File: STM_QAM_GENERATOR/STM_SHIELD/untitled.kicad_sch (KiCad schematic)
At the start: 1 part, among them U1 NUCLEO-F446RE

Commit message: STM_SHIELD_DONE
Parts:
- added D1, D2, D3, D4: LED, LED_SMD:LED_0603_1608Metric_Pad1.05x0.95mm_HandSolder, symbol Device:LED
- added J3: Conn_01x08_Socket, Connector_PinSocket_2.54mm:PinSocket_1x08_P2.54mm_Vertical, symbol Connector:Conn_01x08_Socket
- added R28, R29, R30, R31: R, Resistor_SMD:R_0603_1608Metric_Pad0.98x0.95mm_HandSolder, symbol Device:R
- added R35: DNP, Resistor_SMD:R_0603_1608Metric_Pad0.98x0.95mm_HandSolder, symbol Device:R
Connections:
- net CN6_GND is gone; now on net CN10_GND: U1.CN6_6 (CN6_GND), U1.CN6_7 (CN6_GND)
- net CN7_GND is gone; now on net CN10_GND: U1.CN7_19 (CN7_GND), U1.CN7_20 (CN7_GND), U1.CN7_22 (CN7_GND), U1.CN7_8 (CN7_GND)
- net CN10_GND: now also U1.CN5_7 (CN5_GND), R28.1, R29.1, R30.1, R31.1, R35.2
- net at U1.CN5_1 (D8): now also J3.8 (Pin_8)
- net at U1.CN5_10 (D15): now also J3.1 (Pin_1)
- net at U1.CN5_2 (D9): now also J3.7 (Pin_7)
- net at U1.CN5_3 (D10): now also J3.6 (Pin_6)
- net at U1.CN5_4 (D11): now also J3.5 (Pin_5)
- net at U1.CN5_5 (D12): now also J3.4 (Pin_4)
- net at U1.CN5_6 (D13): now also J3.3 (Pin_3)
- net at U1.CN5_9 (D14): now also J3.2 (Pin_2)
- net +5V: now reaches U1.CN6_5 (CN6_+5V)
- net RX/TX: now reaches U1.CN10_1 (PC9)
- net DAC_Q: now reaches U1.CN10_11 (PA5)
- net at U1.CN10_22 (PB2): now also D2.2 (A)
- net at U1.CN10_24 (PB1): now also D1.2 (A)
- net at U1.CN10_27 (PB4): now also D4.2 (A)
- net at U1.CN10_31 (PB3): now also D3.2 (A)
- net at U1.CN10_32 (AGND): now also R35.1
- net ADC_I: now reaches U1.CN7_28 (PA0)
- net ADC_Q: now reaches U1.CN7_30 (PA1)
- net DAC_I: now reaches U1.CN7_32 (PA4)
- new net: D4.1 (K), R31.2
- new net: D2.1 (K), R29.2
- new net: D3.1 (K), R30.2
- new net: D1.1 (K), R28.2

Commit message: Added values to schematics
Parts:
- R28, R29, R30, R31: value R -> 470
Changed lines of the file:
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@@
 			)
 		)
-		(property "Value" "R"
+		(property "Value" "470"
 			(at 114.3 82.55 90)
 			(effects
@@
 			)
 		)
-		(property "Value" "R"
+		(property "Value" "470"
 			(at 114.3 77.47 90)
 			(effects
@@
 			)
 		)
-		(property "Value" "R"
+		(property "Value" "470"
 			(at 114.3 74.93 90)
 			(effects
@@
 			)
 		)
-		(property "Value" "R"
+		(property "Value" "470"
 			(at 114.3 80.01 90)
 			(effects

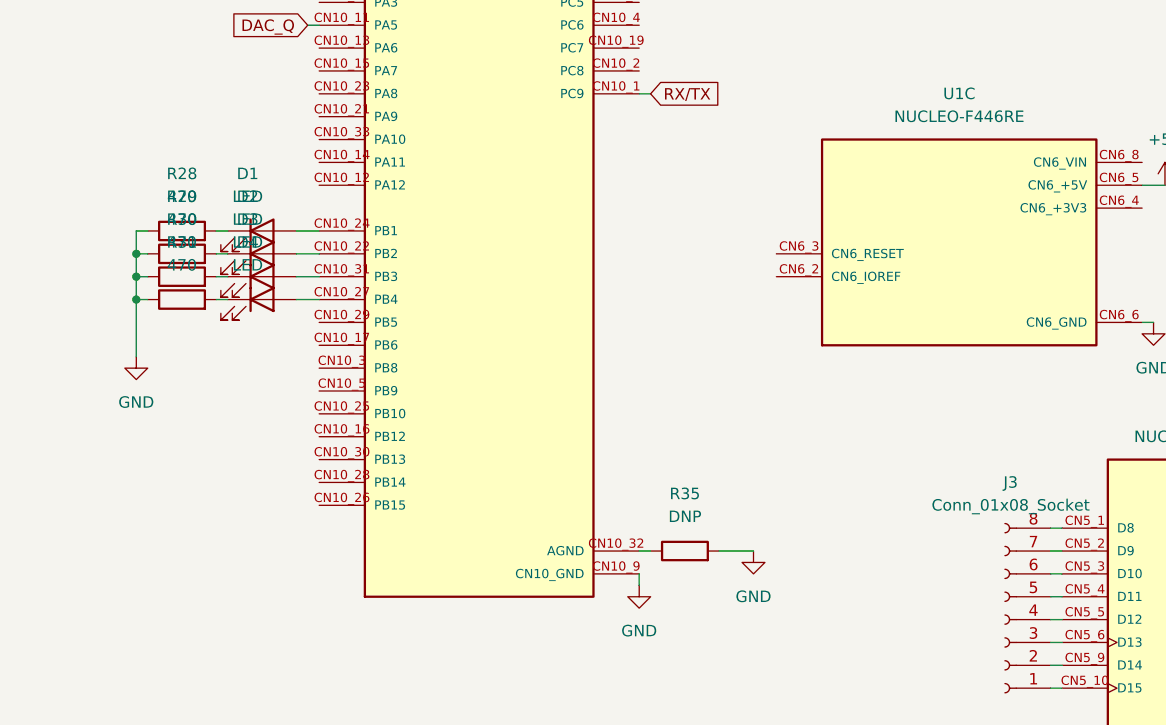
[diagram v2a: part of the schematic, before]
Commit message: STM ADC/DAC test scripts calibrated
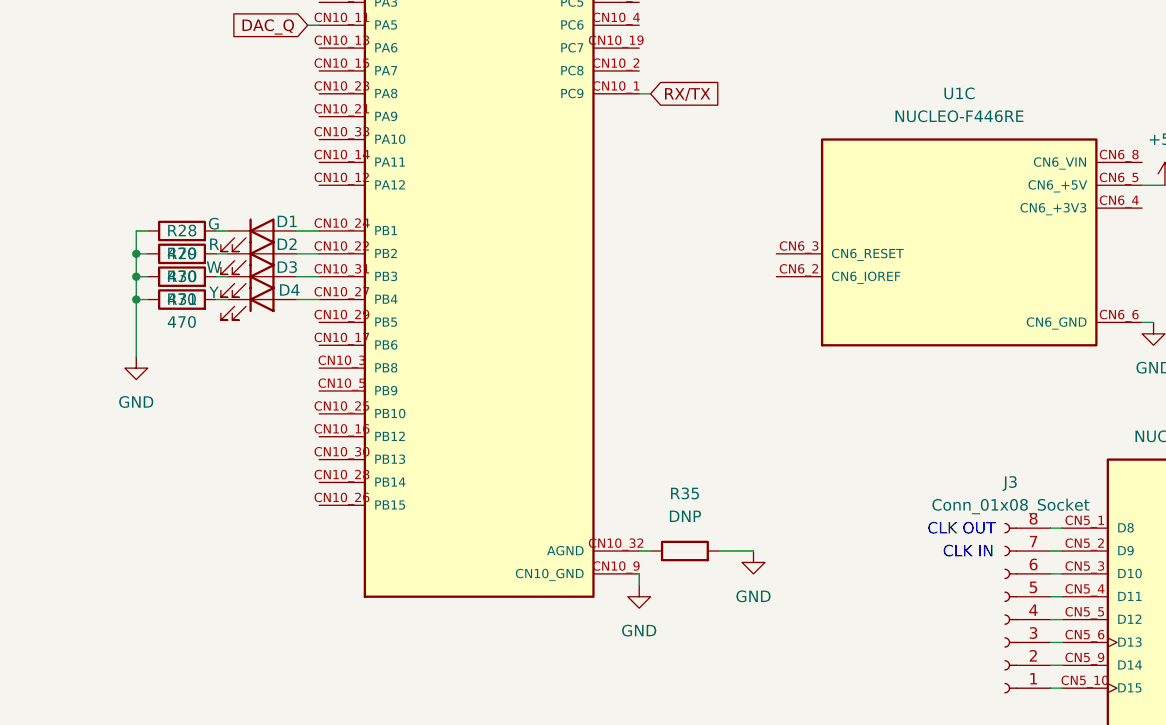
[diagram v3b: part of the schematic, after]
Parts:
- D1: value LED -> G
- D2: value LED -> R
- D3: value LED -> W
- D4: value LED -> Y
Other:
- note added: "CLK IN"
- note added: "CLK OUT"
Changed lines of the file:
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@@
 	(generator_version "9.0")
 	(paper "A4")
+	(text "CLK IN"
+		(exclude_from_sim no)
+		(at 201.676 114.554 0)
+		(effects
+			(font
+				(size 1.27 1.27)
+			)
+		)
+	)
+	(text "CLK OUT"
+		(exclude_from_sim no)
+		(at 200.914 112.014 0)
+		(effects
+			(font
+				(size 1.27 1.27)
+			)
+		)
+	)
 	(junction
 		(at 109.22 86.36)
@@
 		(on_board yes)
 		(dnp no)
-		(fields_autoplaced yes)
 		(property "Reference" "R31"
-			(at 114.3 80.01 90)
+			(at 114.3 86.36 90)
 			(effects
 				(font
@@
 		)
 		(property "Value" "470"
-			(at 114.3 82.55 90)
+			(at 114.3 88.9 90)
 			(effects
 				(font
@@
 		(on_board yes)
 		(dnp no)
-		(fields_autoplaced yes)
 		(property "Reference" "D2"
-			(at 121.6025 74.93 0)
+			(at 125.984 80.264 0)
 			(effects
 				(font
@@
 			)
 		)
-		(property "Value" "LED"
-			(at 121.6025 77.47 0)
+		(property "Value" "R"
+			(at 117.856 80.264 0)
 			(effects
 				(font
@@
 		(on_board yes)
 		(dnp no)
-		(fields_autoplaced yes)
 		(property "Reference" "D3"
-			(at 121.6025 77.47 0)
+			(at 125.984 82.804 0)
 			(effects
 				(font
@@
 			)
 		)
-		(property "Value" "LED"
-			(at 121.6025 80.01 0)
+		(property "Value" "W"
+			(at 117.856 82.804 0)
 			(effects
 				(font
@@
 		(on_board yes)
 		(dnp no)
-		(fields_autoplaced yes)
 		(property "Reference" "D1"
-			(at 121.6025 72.39 0)
+			(at 125.984 77.724 0)
 			(effects
 				(font
@@
 			)
 		)
-		(property "Value" "LED"
-			(at 121.6025 74.93 0)
+		(property "Value" "G"
+			(at 117.856 77.978 0)
 			(effects
 				(font
@@
 		(on_board yes)
 		(dnp no)
-		(fields_autoplaced yes)
 		(property "Reference" "R29"
-			(at 114.3 74.93 90)
+			(at 114.3 81.28 90)
 			(effects
 				(font
@@
 		)
 		(property "Value" "470"
-			(at 114.3 77.47 90)
+			(at 114.3 83.82 90)
 			(effects
 				(font
@@
 		(on_board yes)
 		(dnp no)
-		(fields_autoplaced yes)
 		(property "Reference" "D4"
-			(at 121.6025 80.01 0)
+			(at 126.238 85.344 0)
 			(effects
 				(font
@@
 			)
 		)
-		(property "Value" "LED"
-			(at 121.6025 82.55 0)
+		(property "Value" "Y"
+			(at 117.856 85.598 0)
 			(effects
 				(font
@@
 		(on_board yes)
 		(dnp no)
-		(fields_autoplaced yes)
 		(property "Reference" "R28"
-			(at 114.3 72.39 90)
+			(at 114.3 78.74 90)
 			(effects
 				(font
@@
 		)
 		(property "Value" "470"
-			(at 114.3 74.93 90)
+			(at 114.3 81.28 90)
 			(effects
 				(font
@@
 		(on_board yes)
 		(dnp no)
-		(fields_autoplaced yes)
 		(property "Reference" "R30"
-			(at 114.3 77.47 90)
+			(at 114.3 83.82 90)
 			(effects
 				(font
@@
 		)
 		(property "Value" "470"
-			(at 114.3 80.01 90)
+			(at 114.3 86.36 90)
 			(effects
 				(font
